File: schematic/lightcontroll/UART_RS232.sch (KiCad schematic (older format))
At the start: 9 parts, among them J18 DB9_Female_MountingHoles, U1 74HC14, U7 MAX232

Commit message: save Version 1.0
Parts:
- C1, C3, C33, C4, C5: value 1 uF -> 1uF; Mouser (none) -> https://www.mouser.de/ProductDetail/Wurth-Elektronik/885012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
- C2: Mouser (none) -> https://www.mouser.de/ProductDetail/Wurth-Elektronik/885012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
- J18: Mouser (none) -> https://www.mouser.de/ProductDetail/NorComp/182-009-113R561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
- U1: Mouser (none) -> https://www.mouser.de/ProductDetail/Texas-Instruments/CD74H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
- U7: Mouser (none) -> https://www.mouser.de/ProductDetail/Texas-Instruments/MAX23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
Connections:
- no-connect marks 6 -> 12
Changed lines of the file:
@@
 AR Path="/5EA64CCD/5EA6D925" Ref="C33"  Part="1"
 F 0 "C33" V 3725 3150 50  0000 C CNN
-F 1 "1 uF" V 3816 3150 50  0000 C CNN
+F 1 "1uF" V 3816 3150 50  0000 C CNN
 F 2 "Capacitor_SMD:C_0603_1608Metric_Pad1.05x0.95mm_HandSolder" H 3950 3150 50  0001 C CNN
 F 3 "~" H 3950 3150 50  0001 C CNN
+F 4 "https://www.mouser.de/ProductDetail/Wurth-Elektronik/885012206052?qs=0KOYDY2FL2%2F2JKabApojcQ%3D%3D" H 3950 3150 50  0001 C CNN "Mouser"
 	1    3950 3150
 	0    1    1    0
@@
 AR Path="/5EA64CCD/5EA6D92D" Ref="C5"  Part="1"
 F 0 "C5" V 4375 2850 50  0000 C CNN
-F 1 "1 uF" V 4284 2850 50  0000 C CNN
+F 1 "1uF" V 4284 2850 50  0000 C CNN
 F 2 "Capacitor_SMD:C_0603_1608Metric_Pad1.05x0.95mm_HandSolder" H 4150 2850 50  0001 C CNN
 F 3 "~" H 4150 2850 50  0001 C CNN
+F 4 "https://www.mouser.de/ProductDetail/Wurth-Elektronik/885012206052?qs=0KOYDY2FL2%2F2JKabApojcQ%3D%3D" H 4150 2850 50  0001 C CNN "Mouser"
 	1    4150 2850
 	0    -1   -1   0
@@
 AR Path="/5EA64CCD/5EA6D933" Ref="C4"  Part="1"
 F 0 "C4" H 4168 2546 50  0000 L CNN
-F 1 "1 uF" H 4168 2455 50  0000 L CNN
+F 1 "1uF" H 4168 2455 50  0000 L CNN
 F 2 "Capacitor_SMD:C_0603_1608Metric_Pad1.05x0.95mm_HandSolder" H 4088 2350 50  0001 C CNN
 F 3 "~" H 4050 2500 50  0001 C CNN
+F 4 "https://www.mouser.de/ProductDetail/Wurth-Elektronik/885012206052?qs=0KOYDY2FL2%2F2JKabApojcQ%3D%3D" H 4050 2500 50  0001 C CNN "Mouser"
 	1    4050 2500
 	1    0    0    -1
@@
 AR Path="/5EA64CCD/5EA6D939" Ref="C3"  Part="1"
 F 0 "C3" H 1968 2546 50  0000 L CNN
-F 1 "1 uF" H 1968 2455 50  0000 L CNN
+F 1 "1uF" H 1968 2455 50  0000 L CNN
 F 2 "Capacitor_SMD:C_0603_1608Metric_Pad1.05x0.95mm_HandSolder" H 1888 2350 50  0001 C CNN
 F 3 "~" H 1850 2500 50  0001 C CNN
+F 4 "https://www.mouser.de/ProductDetail/Wurth-Elektronik/885012206052?qs=0KOYDY2FL2%2F2JKabApojcQ%3D%3D" H 1850 2500 50  0001 C CNN "Mouser"
 	1    1850 2500
 	1    0    0    -1
@@
 AR Path="/5EA64CCD/5EA6D96F" Ref="C1"  Part="1"
 F 0 "C1" H 3868 1996 50  0000 L CNN
-F 1 "1 uF" H 3868 1905 50  0000 L CNN
+F 1 "1uF" H 3868 1905 50  0000 L CNN
 F 2 "Capacitor_SMD:C_0603_1608Metric_Pad1.05x0.95mm_HandSolder" H 3788 1800 50  0001 C CNN
 F 3 "~" H 3750 1950 50  0001 C CNN
+F 4 "https://www.mouser.de/ProductDetail/Wurth-Elektronik/885012206052?qs=0KOYDY2FL2%2F2JKabApojcQ%3D%3D" H 3750 1950 50  0001 C CNN "Mouser"
 	1    3750 1950
 	1    0    0    -1
@@
 F 2 "Package_SO:SOP-16_4.55x10.3mm_P1.27mm" H 3200 2200 50  0001 L CNN
 F 3 "http://www.ti.com/lit/ds/symlink/max232.pdf" H 3150 3350 50  0001 C CNN
+F 4 "https://www.mouser.de/ProductDetail/Texas-Instruments/MAX232DR?qs=sGAEpiMZZMtYFXwiBRPs0zIa5BEZai5M" H 3150 3250 50  0001 C CNN "Mouser"
 	1    3150 3250
 	1    0    0    -1
@@
 F 2 "Connector_Dsub:DSUB-9_Male_Horizontal_P2.77x2.84mm_EdgePinOffset7.70mm_Housed_MountingHolesOffset9.12mm" H 6400 3600 50  0001 C CNN
 F 3 " ~" H 6400 3600 50  0001 C CNN
+F 4 "https://www.mouser.de/ProductDetail/NorComp/182-009-113R561?qs=q2eLhcXmQbik7hG6NHalhA%3D%3D" H 6400 3600 50  0001 C CNN "Mouser"
 	1    6400 3600
 	1    0    0    -1
@@
 F 2 "Package_SO:SOIC-14_3.9x8.7mm_P1.27mm" H 1800 5500 50  0001 C CNN
 F 3 "http://www.ti.com/lit/gpn/sn74HC14" H 1800 5500 50  0001 C CNN
+F 4 "https://www.mouser.de/ProductDetail/Texas-Instruments/CD74HCT14M96E4?qs=sGAEpiMZZMutXGli8Ay4kIw6S1qvfJXbLnHR5ePq5ns%3D" H 1800 5500 50  0001 C CNN "Mouser"
 	1    1800 5500
 	1    0    0    -1
@@
 F 2 "Package_SO:SOIC-14_3.9x8.7mm_P1.27mm" H 2400 5500 50  0001 C CNN
 F 3 "http://www.ti.com/lit/gpn/sn74HC14" H 2400 5500 50  0001 C CNN
+F 4 "https://www.mouser.de/ProductDetail/Texas-Instruments/CD74HCT14M96E4?qs=sGAEpiMZZMutXGli8Ay4kIw6S1qvfJXbLnHR5ePq5ns%3D" H 2400 5500 50  0001 C CNN "Mouser"
 	2    2400 5500
 	1    0    0    -1
@@
 F 2 "Package_SO:SOIC-14_3.9x8.7mm_P1.27mm" H 1800 6400 50  0001 C CNN
 F 3 "http://www.ti.com/lit/gpn/sn74HC14" H 1800 6400 50  0001 C CNN
+F 4 "https://www.mouser.de/ProductDetail/Texas-Instruments/CD74HCT14M96E4?qs=sGAEpiMZZMutXGli8Ay4kIw6S1qvfJXbLnHR5ePq5ns%3D" H 1800 6400 50  0001 C CNN "Mouser"
 	4    1800 6400
 	1    0    0    -1
@@
 F 2 "Package_SO:SOIC-14_3.9x8.7mm_P1.27mm" H 2400 5950 50  0001 C CNN
 F 3 "http://www.ti.com/lit/gpn/sn74HC14" H 2400 5950 50  0001 C CNN
+F 4 "https://www.mouser.de/ProductDetail/Texas-Instruments/CD74HCT14M96E4?qs=sGAEpiMZZMutXGli8Ay4kIw6S1qvfJXbLnHR5ePq5ns%3D" H 2400 5950 50  0001 C CNN "Mouser"
 	5    2400 5950
 	1    0    0    -1
@@
 F 2 "Package_SO:SOIC-14_3.9x8.7mm_P1.27mm" H 1800 5950 50  0001 C CNN
 F 3 "http://www.ti.com/lit/gpn/sn74HC14" H 1800 5950 50  0001 C CNN
+F 4 "https://www.mouser.de/ProductDetail/Texas-Instruments/CD74HCT14M96E4?qs=sGAEpiMZZMutXGli8Ay4kIw6S1qvfJXbLnHR5ePq5ns%3D" H 1800 5950 50  0001 C CNN "Mouser"
 	6    1800 5950
 	1    0    0    -1
@@
 F 2 "Package_SO:SOIC-14_3.9x8.7mm_P1.27mm" H 9000 1950 50  0001 C CNN
 F 3 "http://www.ti.com/lit/gpn/sn74HC14" H 9000 1950 50  0001 C CNN
+F 4 "https://www.mouser.de/ProductDetail/Texas-Instruments/CD74HCT14M96E4?qs=sGAEpiMZZMutXGli8Ay4kIw6S1qvfJXbLnHR5ePq5ns%3D" H 9000 1950 50  0001 C CNN "Mouser"
 	7    9000 1950
 	1    0    0    -1
@@
 F 2 "Package_SO:SOIC-14_3.9x8.7mm_P1.27mm" H 1800 6950 50  0001 C CNN
 F 3 "http://www.ti.com/lit/gpn/sn74HC14" H 1800 6950 50  0001 C CNN
+F 4 "https://www.mouser.de/ProductDetail/Texas-Instruments/CD74HCT14M96E4?qs=sGAEpiMZZMutXGli8Ay4kIw6S1qvfJXbLnHR5ePq5ns%3D" H 1800 6950 50  0001 C CNN "Mouser"
 	3    1800 6950
 	1    0    0    -1
@@
 F 2 "Capacitor_SMD:C_0603_1608Metric_Pad1.05x0.95mm_HandSolder" H 9650 1950 50  0001 C CNN
 F 3 "~" H 9650 1950 50  0001 C CNN
+F 4 "https://www.mouser.de/ProductDetail/Wurth-Elektronik/885012206071?qs=0KOYDY2FL2%2FEBQkuHgvarg%3D%3D" H 9650 1950 50  0001 C CNN "Mouser"
 	1    9650 1950
 	1    0    0    -1
@@
 P 6400 4200
 AR Path="/5C906D74/5ED755D7" Ref="#PWR?"  Part="1"
-AR Path="/5EA64CCD/5ED755D7" Ref="#PWR?"  Part="1"
-F 0 "#PWR?" H 6400 3950 50  0001 C CNN
+AR Path="/5EA64CCD/5ED755D7" Ref="#PWR0109"  Part="1"
+F 0 "#PWR0109" H 6400 3950 50  0001 C CNN
 F 1 "GNDREF" H 6405 4027 50  0000 C CNN
 F 2 "" H 6400 4200 50  0001 C CNN
@@
 	1    0    0    -1
 $EndComp
+NoConn ~ 6100 3200
+NoConn ~ 6100 3300
+NoConn ~ 6100 3500
+NoConn ~ 6100 3700
+NoConn ~ 6100 3800
+NoConn ~ 6100 3900
 $EndSCHEMATC

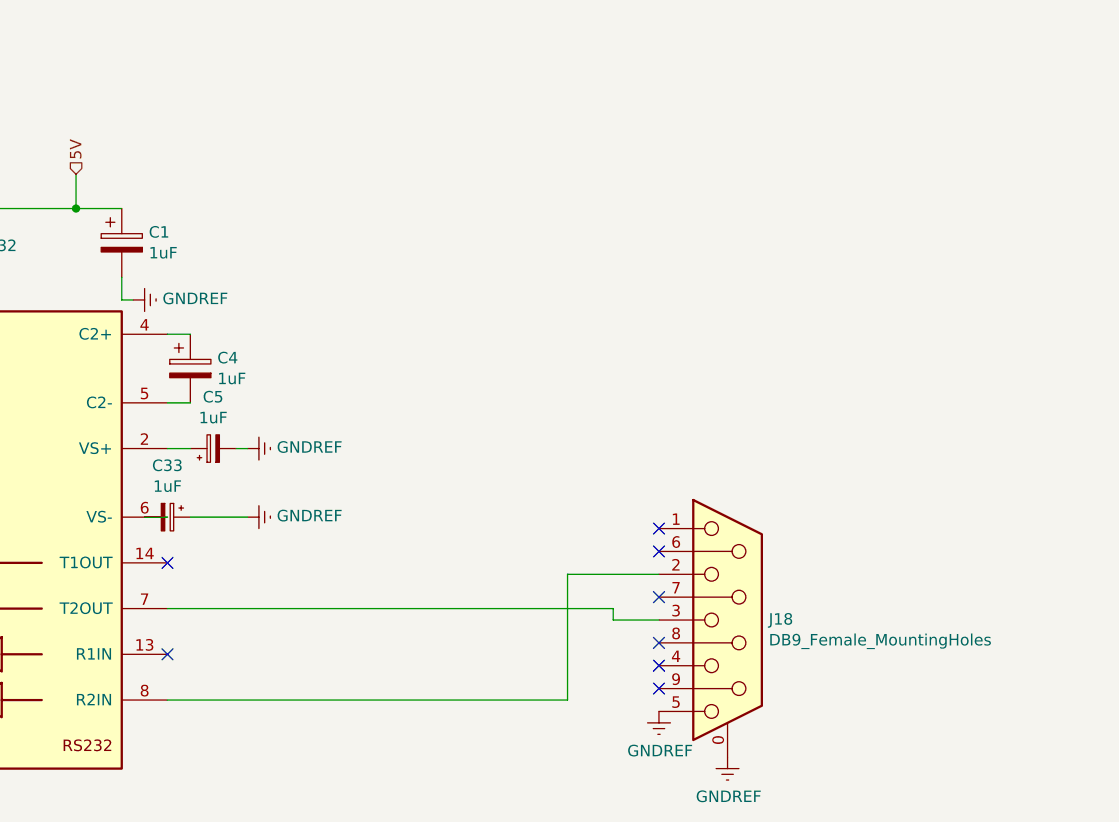
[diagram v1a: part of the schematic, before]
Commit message: Updated PCB to Revision 2.0
- Added an 2.54mm pin header for second RS232 UART, which was already available in rev 1.0
- Changed all 2.00mm pin header to 2.54mm pin header. This fixes the mistake done in selecting the wrong footprint in rev 1.0
- Corrected schematic and layout of the spi to sk2812 circuits. During testing of previous rev some mistakes where found.
	* the second logical schemitac part of 74ls123 changes meaning of pin 6 and 7 compared to 15 and 14 of the first
	* The vibrator for the one signal needs to be also triggered with every rising edge, so use input A instead of binding it to gnd
	* Use the fourth nand to invert clock signal for a input of one vibrator
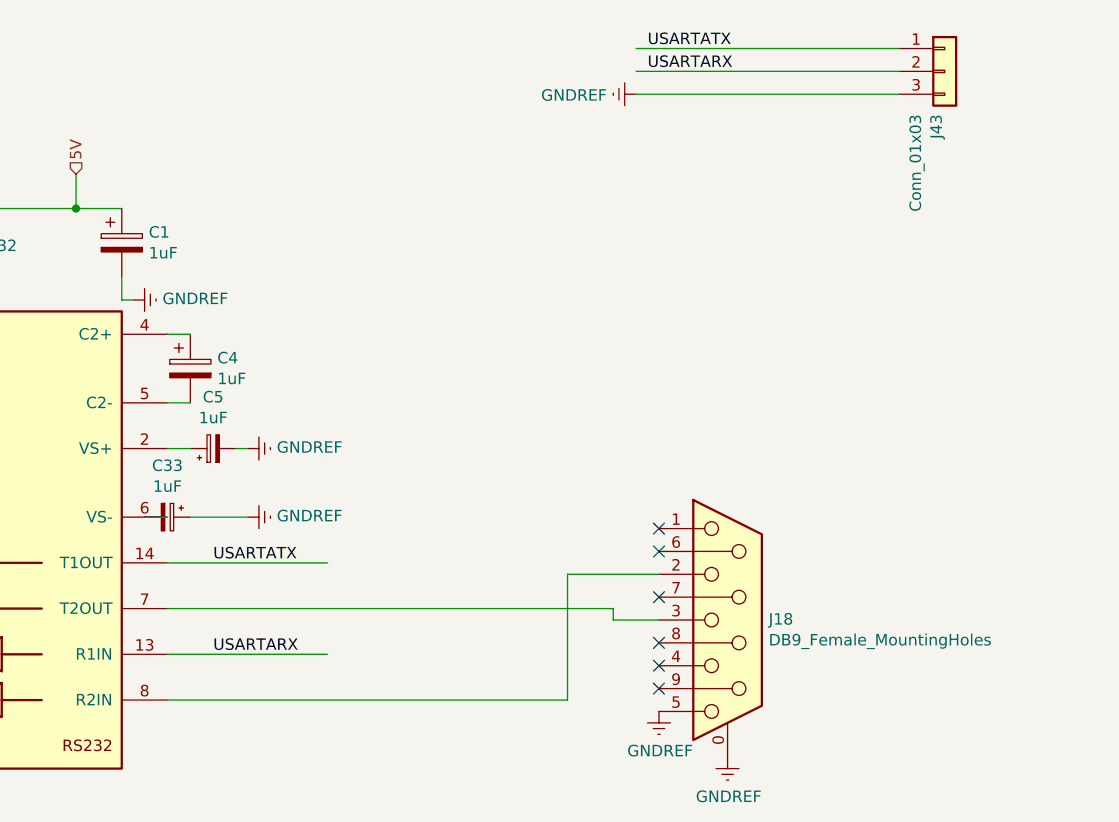
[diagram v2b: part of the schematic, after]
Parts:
- added J43: Conn_01x03, Connector_PinHeader_2.54mm:PinHeader_1x03_P2.54mm_Vertical, symbol Connector_Generic:Conn_01x03
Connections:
- net labels added: USARTARX, USARTATX
- wire segments 36 -> 41
- no-connect marks 12 -> 10
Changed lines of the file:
@@
 Title "UART RS232 Over DSub9"
 Date "2020-05-25"
-Rev "1.1"
+Rev "2.0"
 Comp "Tibersam Industries"
 Comment1 ""
@@
 Text HLabel 1500 3950 0    50   Output ~ 0
 UARTB_RX
-NoConn ~ 3950 3350
-NoConn ~ 3950 3750
 $Comp
 L power:GNDREF #PWR?
@@
 NoConn ~ 6100 3800
 NoConn ~ 6100 3900
+Text Label 4150 3350 0    50   ~ 0
+USARTATX
+Wire Wire Line
+	3950 3750 4650 3750
+Text Label 4150 3750 0    50   ~ 0
+USARTARX
+Wire Wire Line
+	3950 3350 4650 3350
+$Comp
+L Connector_Generic:Conn_01x03 J43
+U 1 1 607A13A2
+P 7350 1200
+F 0 "J43" V 7314 1012 50  0000 R CNN
+F 1 "Conn_01x03" V 7223 1012 50  0000 R CNN
+F 2 "Connector_PinHeader_2.54mm:PinHeader_1x03_P2.54mm_Vertical" H 7350 1200 50  0001 C CNN
+F 3 "~" H 7350 1200 50  0001 C CNN
+	1    7350 1200
+	1    0    0    -1
+$EndComp
+Text Label 6050 1100 0    50   ~ 0
+USARTATX
+Text Label 6050 1200 0    50   ~ 0
+USARTARX
+$Comp
+L power:GNDREF #PWR05
+U 1 1 607A88E1
+P 6000 1300
+F 0 "#PWR05" H 6000 1050 50  0001 C CNN
+F 1 "GNDREF" V 6005 1172 50  0000 R CNN
+F 2 "" H 6000 1300 50  0001 C CNN
+F 3 "" H 6000 1300 50  0001 C CNN
+	1    6000 1300
+	0    1    1    0
+$EndComp
+Wire Wire Line
+	6000 1100 7150 1100
+Wire Wire Line
+	6000 1200 7150 1200
+Wire Wire Line
+	6000 1300 7150 1300
 $EndSCHEMATC
